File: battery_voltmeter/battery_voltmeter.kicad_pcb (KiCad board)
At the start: 2 copper layers, 50 x 20 mm, 12 parts, among them J1 Conn_02x08_Odd_Even, J2 USB_B_Micro, U1 SP420281N, U2 ATSAMD21E18A-A, U3 L7805, U4 AP2112K-3.3

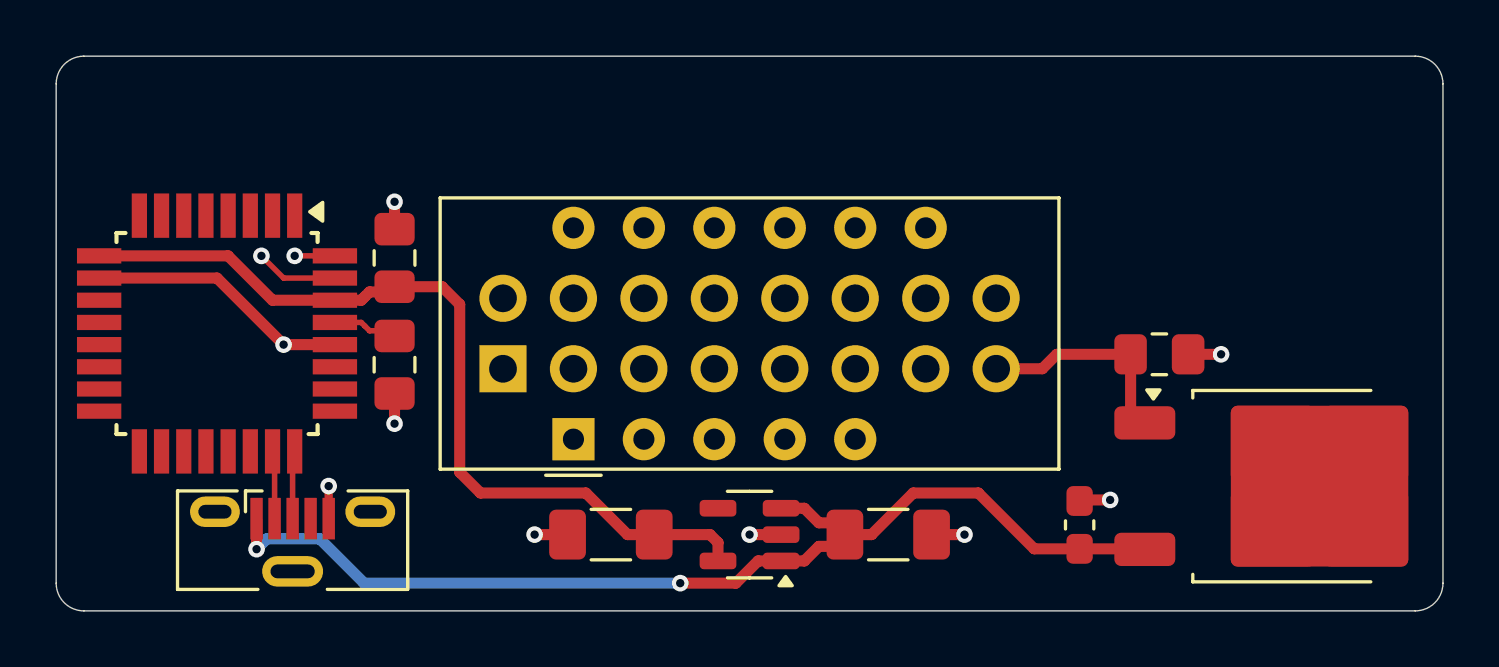
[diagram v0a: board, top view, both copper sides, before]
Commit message: WIP battery voltmeter module: part 2
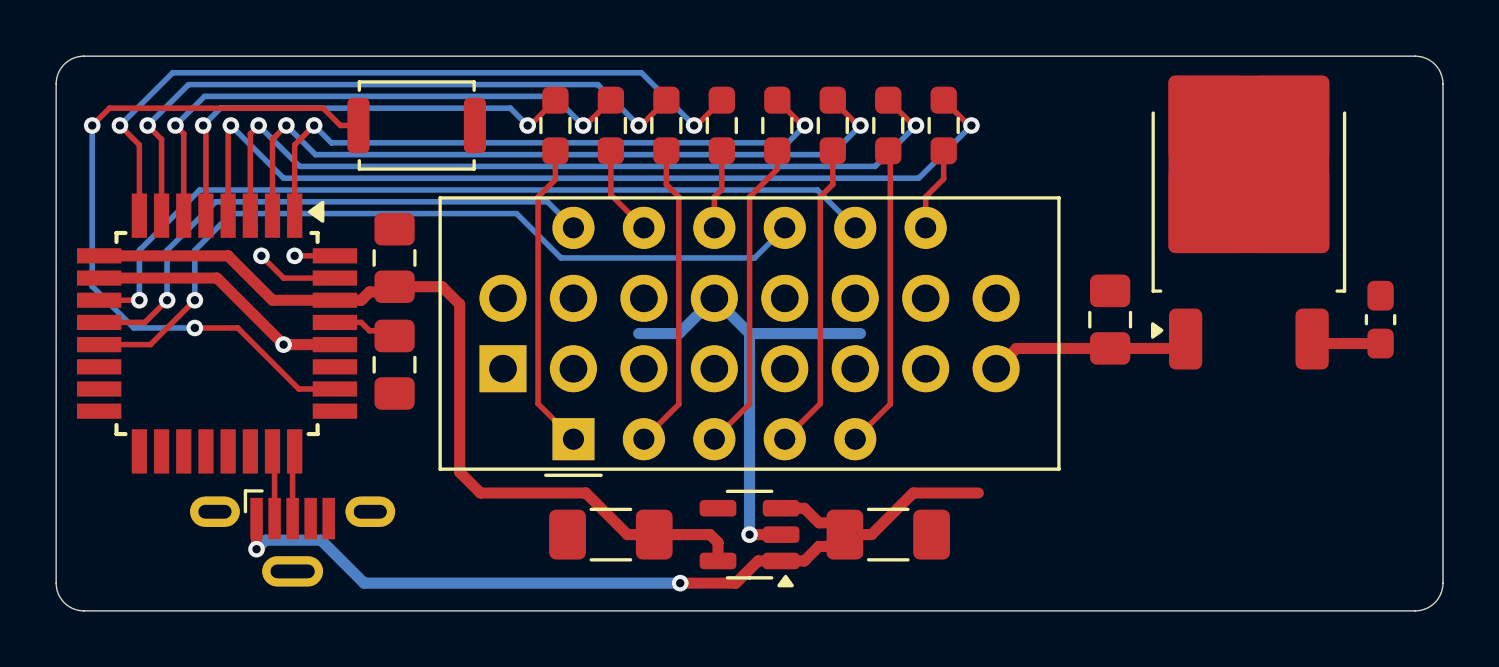
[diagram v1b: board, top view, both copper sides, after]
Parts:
- added R1: 120R, Resistor_SMD:R_0603_1608Metric_Pad0.98x0.95mm_HandSolder, F.Cu at (145.0, 92.5)
- added R2: 120R, Resistor_SMD:R_0603_1608Metric_Pad0.98x0.95mm_HandSolder, F.Cu at (157.0, 92.5)
- added R3: 120R, Resistor_SMD:R_0603_1608Metric_Pad0.98x0.95mm_HandSolder, F.Cu at (153.0, 92.5)
- added R4: 120R, Resistor_SMD:R_0603_1608Metric_Pad0.98x0.95mm_HandSolder, F.Cu at (147.0, 92.5)
- added R5: 120R, Resistor_SMD:R_0603_1608Metric_Pad0.98x0.95mm_HandSolder, F.Cu at (143.0, 92.5)
- added R6: 120R, Resistor_SMD:R_0603_1608Metric_Pad0.98x0.95mm_HandSolder, F.Cu at (149.0, 92.5)
- added R7: 120R, Resistor_SMD:R_0603_1608Metric_Pad0.98x0.95mm_HandSolder, F.Cu at (155.0, 92.5)
- added R8: 120R, Resistor_SMD:R_0603_1608Metric_Pad0.98x0.95mm_HandSolder, F.Cu at (151.0, 92.5)
- added SW1: SKRK, Button_Switch_SMD:SW_Push_SPST_NO_Alps_SKRK, F.Cu at (138.0, 92.5)
- moved C2 13.1 mm to (172.8, 99.5)
- moved U3 10.4 mm to (168.0, 95.2), turned to 90 degrees
- moved C1 2.17 mm to (163.0, 99.5), turned to 90 degrees
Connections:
- U1 pad 1: unconnected-(U1-E-Pad1) -> Net-(U1-E)
- U1 pad 10: unconnected-(U1-F-Pad10) -> Net-(U1-F)
- U1 pad 11: unconnected-(U1-A-Pad11) -> Net-(U1-A)
- U1 pad 12: unconnected-(U1-DIG1-Pad12) -> /DIG1
- U1 pad 2: unconnected-(U1-D-Pad2) -> Net-(U1-D)
- U1 pad 3: unconnected-(U1-DP-Pad3) -> Net-(U1-DP)
- U1 pad 4: unconnected-(U1-C-Pad4) -> Net-(U1-C)
- U1 pad 5: unconnected-(U1-G-Pad5) -> Net-(U1-G)
- U1 pad 7: unconnected-(U1-B-Pad7) -> Net-(U1-B)
- U1 pad 8: unconnected-(U1-DIG3-Pad8) -> /DIG3
- U1 pad 9: unconnected-(U1-DIG2-Pad9) -> /DIG2
- U2 pad 1: unconnected-(U2-PA00-Pad1) -> /DP
- U2 pad 11: unconnected-(U2-PA08-Pad11) -> /DIG3
- U2 pad 12: unconnected-(U2-PA09-Pad12) -> /DIG1
- U2 pad 13: unconnected-(U2-PA10-Pad13) -> /DIG2
- U2 pad 2: unconnected-(U2-PA01-Pad2) -> /C
- U2 pad 26: unconnected-(U2-~{RESET}-Pad26) -> /~{RESET}
- U2 pad 3: unconnected-(U2-PA02-Pad3) -> /G
- U2 pad 4: unconnected-(U2-PA03-Pad4) -> /B
- U2 pad 5: unconnected-(U2-PA04-Pad5) -> /E
- U2 pad 6: unconnected-(U2-PA05-Pad6) -> /A
- U2 pad 7: unconnected-(U2-PA06-Pad7) -> /D
- U2 pad 8: unconnected-(U2-PA07-Pad8) -> /F
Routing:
- net /B: track 0.00 -> 32.9 mm, vias 0 -> 2
- net /DIG3: track 0.00 -> 30.5 mm, vias 0 -> 1
- net /G: track 0.00 -> 29.7 mm, vias 0 -> 2
- net /DIG2: track 0.00 -> 28.8 mm, vias 0 -> 1
- net /F: track 0.00 -> 27.2 mm, vias 0 -> 2
- net /C: track 0.00 -> 26.4 mm, vias 0 -> 2
- net /~{RESET}: track 0.00 -> 26.2 mm, vias 0 -> 2
- net /D: track 0.00 -> 23.8 mm, vias 0 -> 2
- net /DP: track 0.00 -> 23.1 mm, vias 0 -> 2
- net /DIG1: track 0.00 -> 20.3 mm, vias 0 -> 1
- net /A: track 0.00 -> 20.3 mm, vias 0 -> 2
- net /E: track 0.00 -> 16.9 mm, vias 0 -> 2
- net Net-(U1-DP): track 0.00 -> 11.3 mm
- net Net-(U1-E): track 0.00 -> 11.2 mm
- net Net-(U1-C): track 0.00 -> 11.1 mm
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
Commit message: WIP battery voltmeter module: part 3
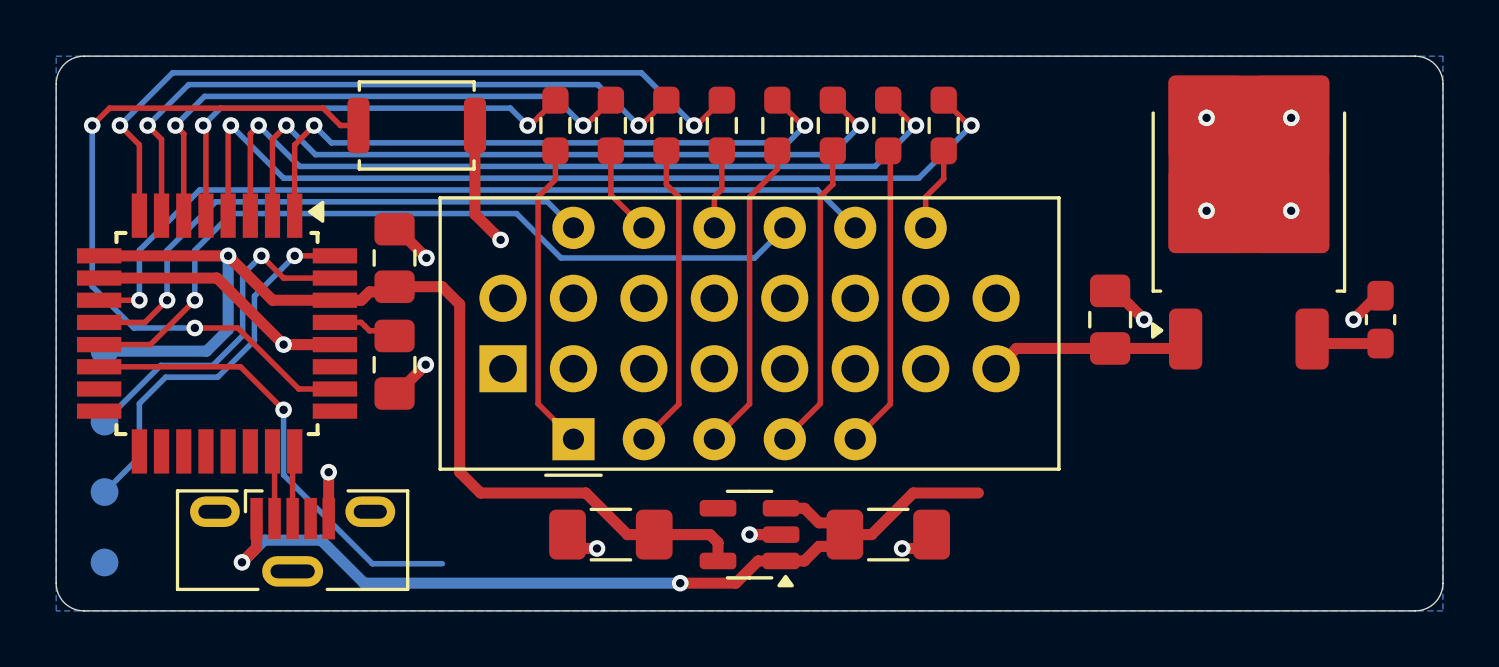
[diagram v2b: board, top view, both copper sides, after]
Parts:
- added TP1: +3V3, TestPoint:TestPoint_Pad_D1.0mm, B.Cu at (126.7, 100.6)
- added TP2: SWCLK, TestPoint:TestPoint_Pad_D1.0mm, B.Cu at (126.7, 103.2)
- added TP3: SWDIO, TestPoint:TestPoint_Pad_D1.0mm, B.Cu at (126.7, 105.7)
- added TP4: GND, TestPoint:TestPoint_Pad_D1.0mm, B.Cu at (126.7, 108.3)
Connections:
- U2 pad 14: unconnected-(U2-PA11-Pad14) -> /V_MEASURE
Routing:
- net /V_MEASURE: track 0.00 -> 16.7 mm, vias 0 -> 1
- net /SWDIO: track 1.45 -> 13.9 mm
- net /SWCLK: track 2.98 -> 12.4 mm
- net +3V3: track 31.2 -> 38.6 mm, vias 0 -> 1
- net GND: track 26.9 -> 25.5 mm, vias 2 -> 14
- net +5V: track 34.5 -> 35.9 mm
- added copper zone on B.Cu, net GND
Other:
- board text added: "3V3"
- board text added: "GND"
- board text added: "SWCLK"
- board text added: "SWDIO"

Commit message: Finish battery voltmeter module
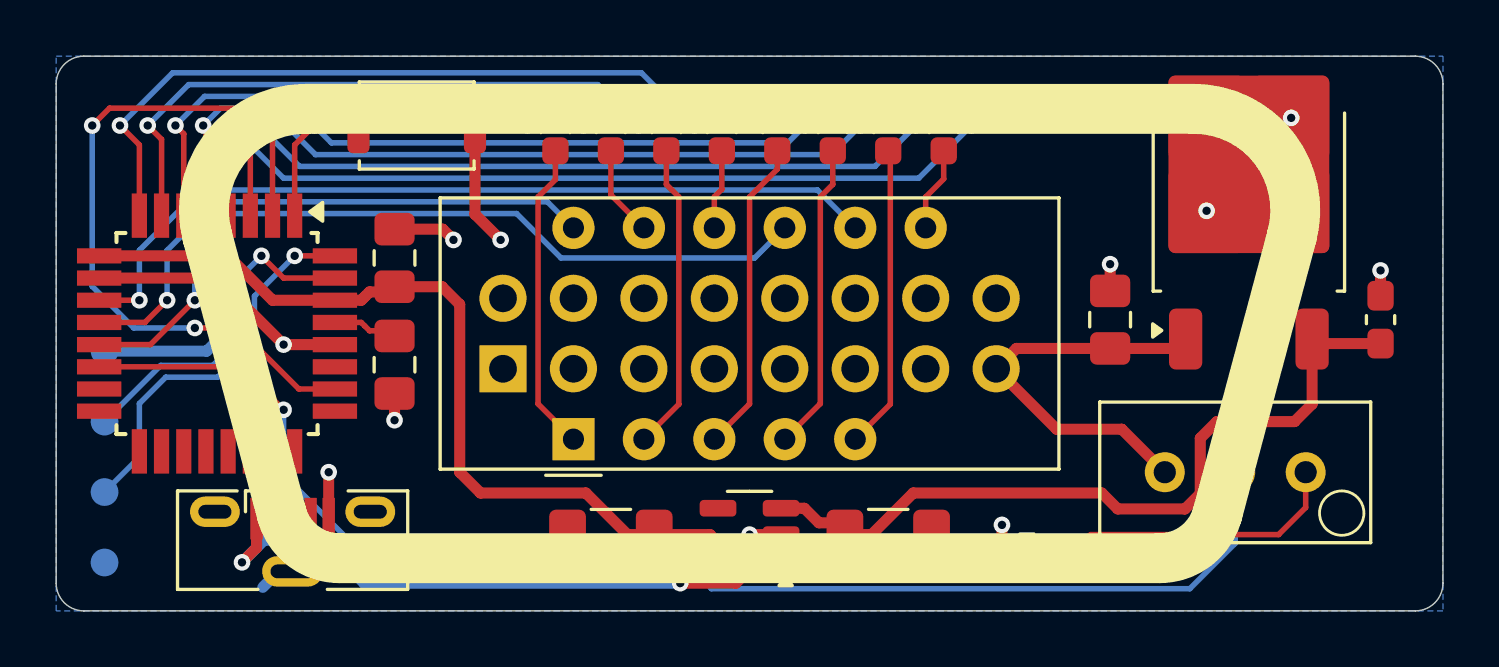
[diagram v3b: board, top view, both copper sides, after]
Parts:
- added R9: 22R, Resistor_SMD:R_0603_1608Metric_Pad0.98x0.95mm_HandSolder, F.Cu at (160.0, 107.8)
- added RV1: 5k, Potentiometer_THT:Potentiometer_Bourns_3296W_Vertical, F.Cu at (170.1, 105.0)
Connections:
- J2 pad 6: unconnected-(J2-Shield-Pad6) -> GND
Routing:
- net /V_MEASURE: track 16.7 -> 48.9 mm
- net +5V: track 35.9 -> 53.2 mm
- net Net-(R9-Pad1): track 0.00 -> 11.0 mm
- net +12V: track 7.28 -> 14.9 mm
- net GND: track 25.5 -> 26.6 mm, vias 14 -> 15
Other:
- board text added: "Battery Voltmeter"

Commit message: Fix component selection issue, add battery voltmeter firmware
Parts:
- R9: value 22R -> 10k
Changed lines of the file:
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@@
 			)
 		)
-		(property "Value" "22R"
+		(property "Value" "10k"
 			(at 0 1.43 180)
 			(layer "F.Fab")
@@
 			)
 		)
-		(property "LCSC" "C23345"
+		(property "LCSC" "C25804"
 			(at 0 0 180)
 			(unlocked yes)

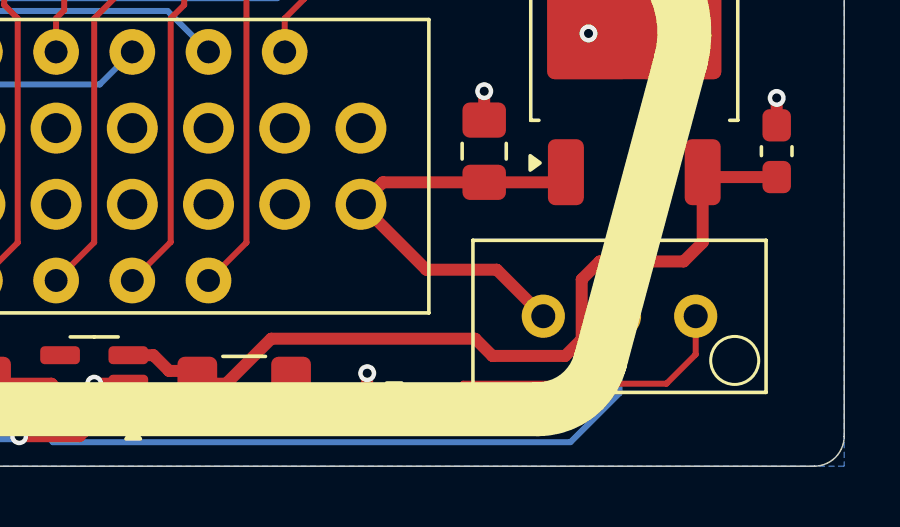
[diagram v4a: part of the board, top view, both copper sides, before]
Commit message: Fix serious voltage divider issue
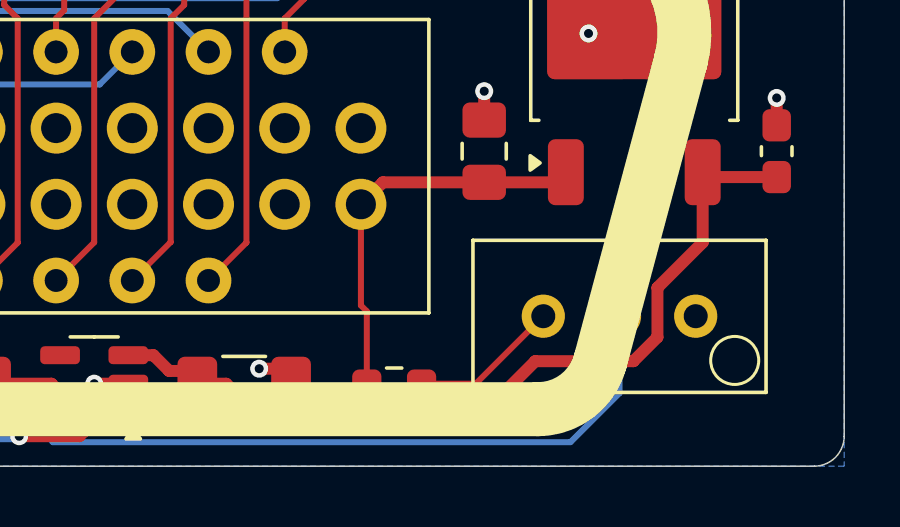
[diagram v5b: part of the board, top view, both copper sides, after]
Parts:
- moved R9 0.50 mm to (160.0, 107.2), turned to 0 degrees
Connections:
- R9 pad 1: Net-(R9-Pad1) -> +12V
- R9 pad 2: GND -> Net-(R9-Pad2)
- RV1 pad 1: Net-(R9-Pad1) -> GND
- RV1 pad 3: +12V -> Net-(R9-Pad2)
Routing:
- net Net-(R9-Pad1): track 11.0 -> 0.00 mm
- net Net-(R9-Pad2): track 0.00 -> 4.99 mm
- net +12V: track 14.9 -> 13.3 mm
- net GND: track 26.6 -> 25.8 mm, vias 15 -> 14
